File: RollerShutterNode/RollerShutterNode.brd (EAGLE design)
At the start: 49.5 x 49.2 mm, 32 parts, among them IC2 AT25DF512C-SSHN-B, U1 MMBT2222A-7-F, U2 MMBT2222A-7-F, U3 LM321

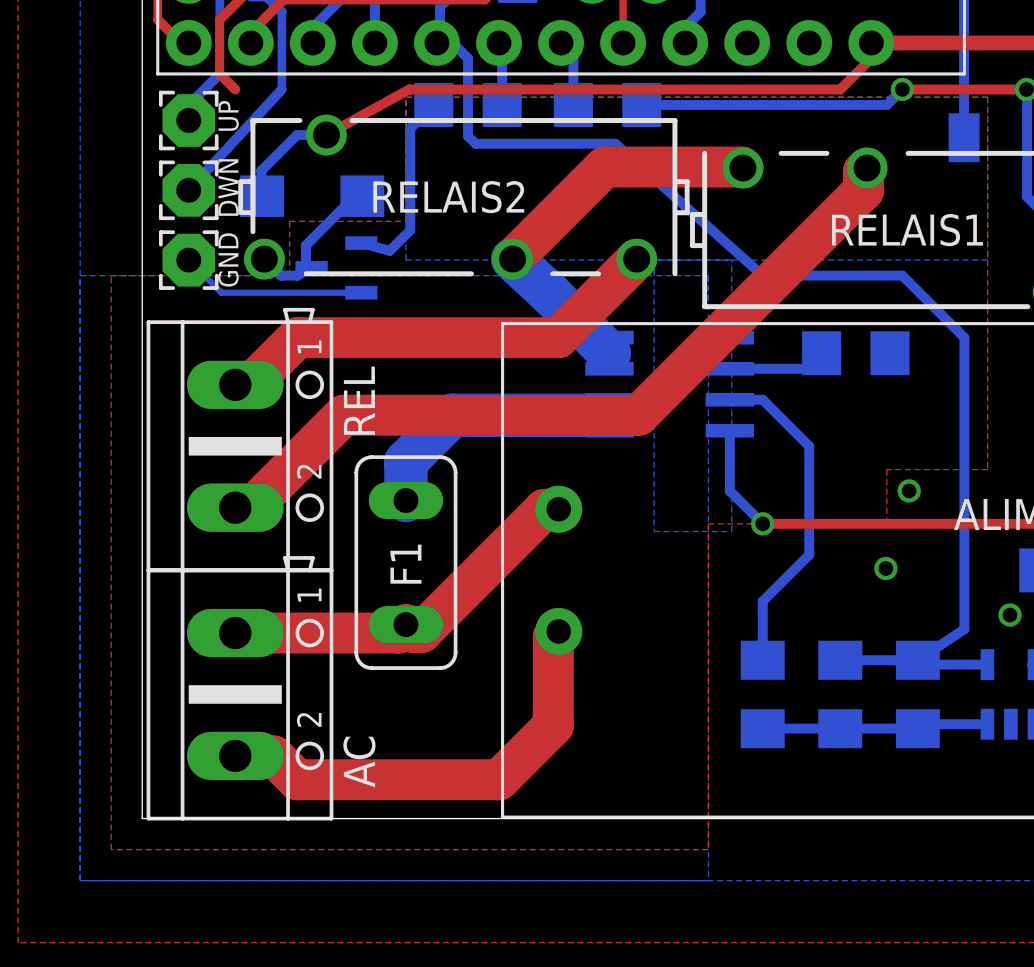
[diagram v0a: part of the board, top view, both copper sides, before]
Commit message: fuse removed, added 12-220v motor control
Need to use external fuse and snubber if needed
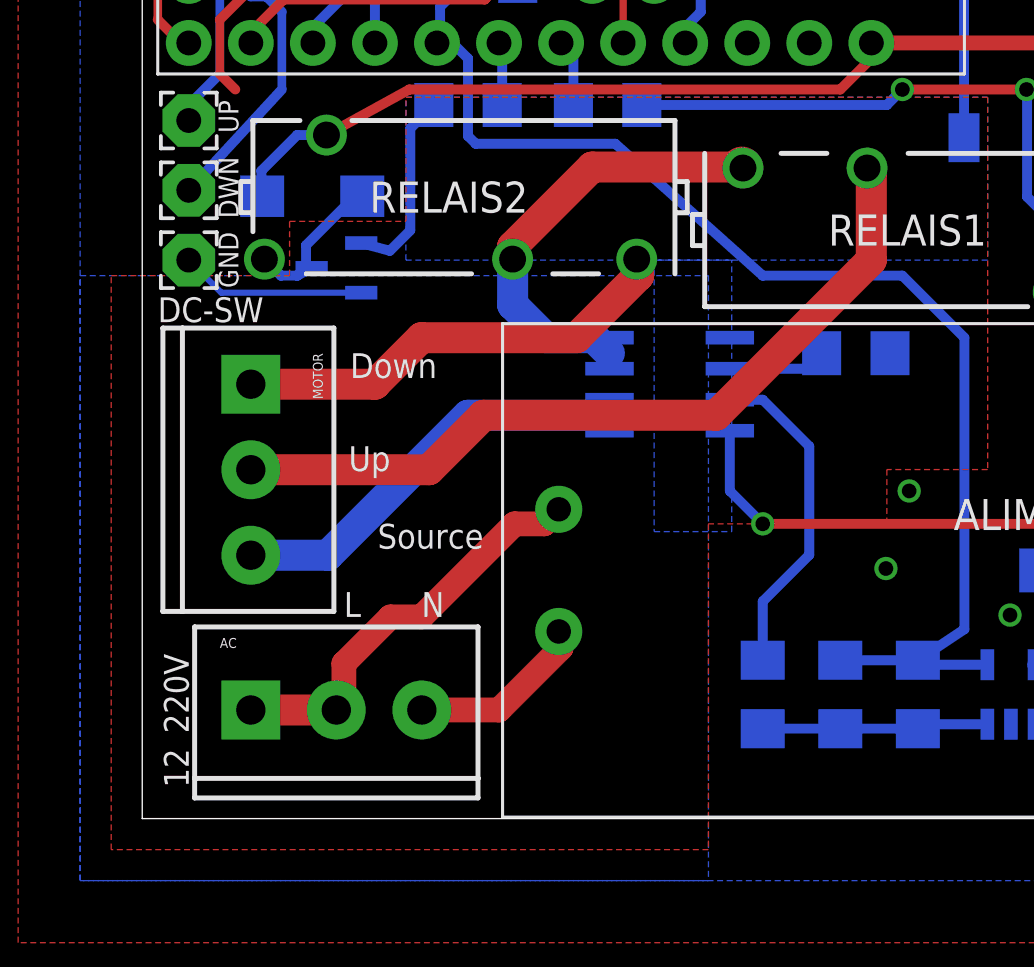
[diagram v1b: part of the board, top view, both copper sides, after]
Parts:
- removed F1: (no value), fuse:TE5
- removed REL: (no value), ProgrammateurFilPilote_1.2:AK500/2
- added MOTOR: (no value), SparkFun-Connectors:SCREWTERMINAL-3.5MM-3
- AC: device ProgrammateurFilPilote_1.2:AK500/2 -> SparkFun-Connectors:SCREWTERMINAL-3.5MM-3
- moved AC 0.90 mm to (4.45, 4.45), turned to 0 degrees
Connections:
- removed net COM_BIS: ACS1.1, ACS1.2, F1.2
- new net 12_220: ACS1.1, ACS1.2, MOTOR.3
- net N$7: now also MOTOR.2; no longer REL.2
- net N$9: now also MOTOR.1; no longer REL.1
- net NEUTRE: now also AC.3; no longer AC.2
- net PHASE: now also AC.2; no longer F1.1
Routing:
- net 12_220: track 0.00 -> 18.3 mm
- net COM_BIS: track 12.0 -> 0.00 mm
- net NEUTRE: track 18.3 -> 7.47 mm
- net COM: track 17.8 -> 19.2 mm
- net PHASE: track 15.6 -> 16.9 mm
- net N$7: track 32.1 -> 32.8 mm
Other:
- board text added: "12_220V"
- board text added: "DC-SW"
- board text added: "Down"
- board text added: "L"
- board text added: "N"
- board text added: "Source"
- board text added: "Up"
